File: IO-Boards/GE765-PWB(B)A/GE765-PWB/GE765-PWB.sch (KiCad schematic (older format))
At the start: 55 parts, among them CN33 B12PSHF1A, CN35 B6P-VH, CN36 B3SHF1AA, U1 74LS175, U10 Ferrite_Bead_Small, U11 Ferrite_Bead_Small, U12 Ferrite_Bead_Small, U13 Ferrite_Bead_Small, U17 Ferrite_Bead_Small, U18 Ferrite_Bead_Small, U19 Ferrite_Bead_Small, U2 74LS175, U20 Ferrite_Bead_Small, U21 Ferrite_Bead_Small, U3 74LS14

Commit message: Updated GE765
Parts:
- added C1: 10uf 16v, Capacitor_THT:CP_Radial_D5.0mm_P2.50mm, symbol Device:CP_Small
- added C3: 0.01uf, Capacitor_THT:C_Disc_D3.0mm_W1.6mm_P2.50mm, symbol Device:C_Small
- added J?: Conn_02x40_Row_Letter_First, symbol Connector_Generic:Conn_02x40_Row_Letter_First
- added R1: 510, Resistor_THT:R_Axial_DIN0204_L3.6mm_D1.6mm_P5.08mm_Horizontal, symbol Device:R_Small
- added R13: 4.7k, Resistor_THT:R_Axial_DIN0204_L3.6mm_D1.6mm_P5.08mm_Horizontal, symbol Device:R_Small
- added R2: 470, Resistor_THT:R_Axial_DIN0204_L3.6mm_D1.6mm_P5.08mm_Horizontal, symbol Device:R_Small
- added U?: MPD4701AG, symbol MOSFET_NEC:MPD4701AG
- 8G: renamed from 8D; value 74LS245 -> 74LCX245
- renumbered U2 to 11C, U1 to 8B
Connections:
- net labels added: 11C-CP, 175-~RST, 6D-CLK-1, 6D-CLK-2, 8B-CP, D0, D1, D2, D3, D4, D5, D6, D7, DQ0, DQ1, DQ2, DQ3, DQ4, DQ5, DQ6, DQ7
- wire segments 128 -> 217
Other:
- moved on the sheet: 10D, 11C, 6D1A, 6D1B, 6D1C, 6D1E, 6D1F, 7B, 8B, 8D, 8G, RN2

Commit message: 50% Complete schematics
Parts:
- added R12: 4.7k, Resistor_THT:R_Axial_DIN0204_L3.6mm_D1.6mm_P5.08mm_Horizontal, symbol Device:R_Small
- RA2: renamed from RN2; value R_Network08 -> 4.7K
- RA4: renamed from RN3; value R_Network08 -> 4.7k
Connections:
- net labels added: 8G-A~B, 8G-~CE, CN31-A15, CN31-A21, CN31-A22, CN31-A6, CN31-B21, CN31-B22, CN31-B23, CN31-B6, D4701-RESET, D4701-U~L, D4701-~CE, D4701-~X~Y
- wire segments 217 -> 266
- no-connect marks 1 -> 28
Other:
- note added: "Output 1"
- note added: "Output 2"
- note added: "Output Driver 1"
- note added: "Output Driver 2"
- moved on the sheet: 10D, 11C, 2G, 3G, 4G, 6D1A, 6D1B, 6D1C, 6D1D, 6D1E, 6D1F, 6E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

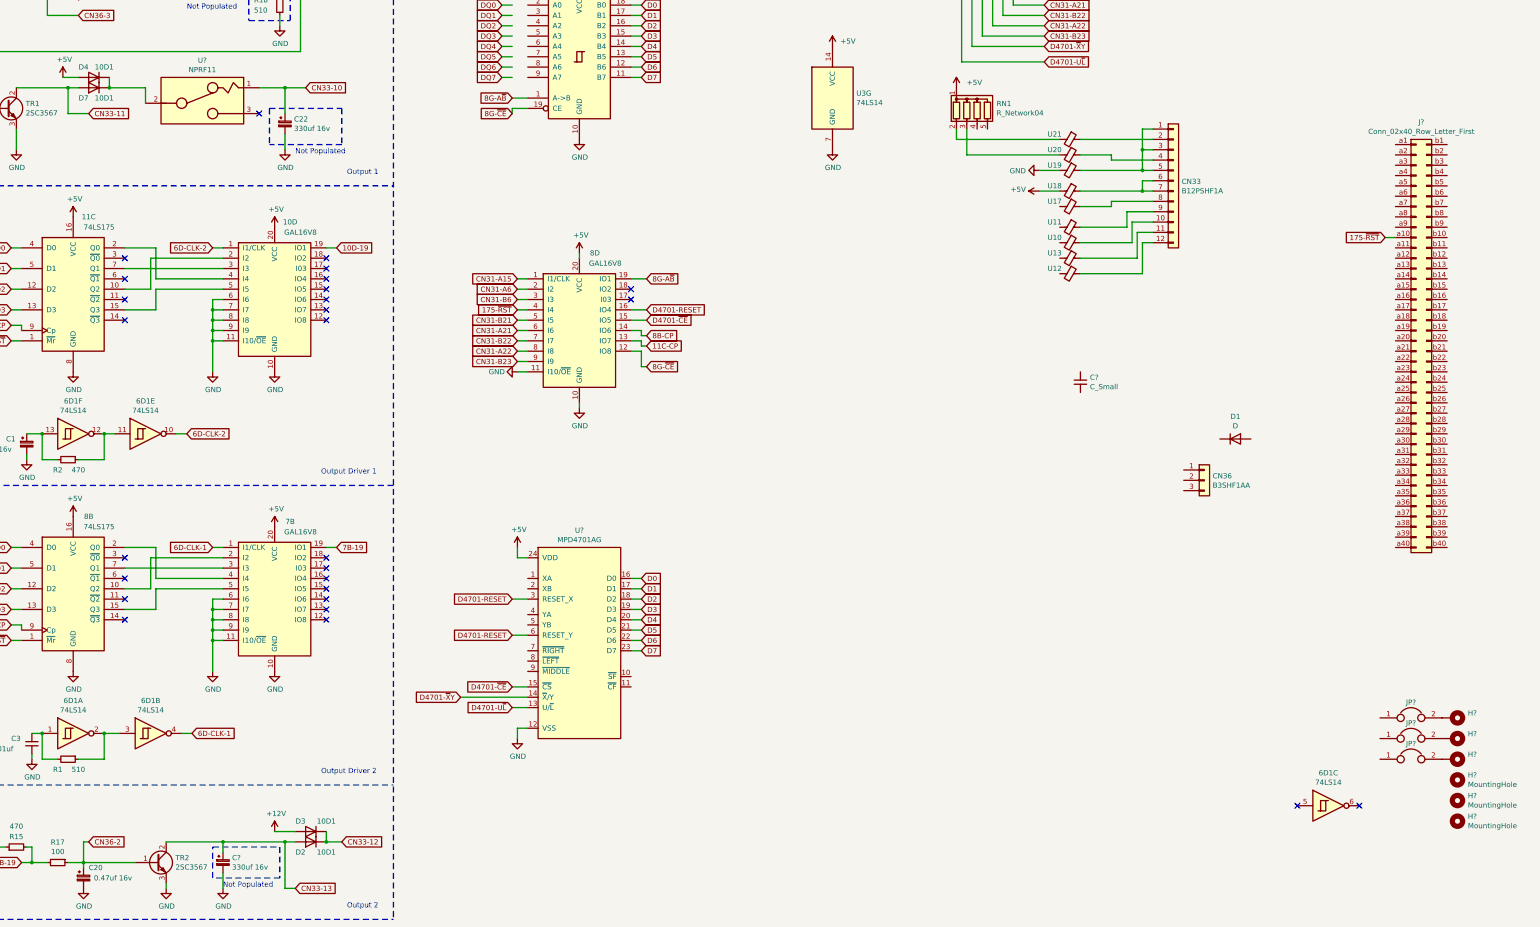
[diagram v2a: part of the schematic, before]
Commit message: Finished reel connector
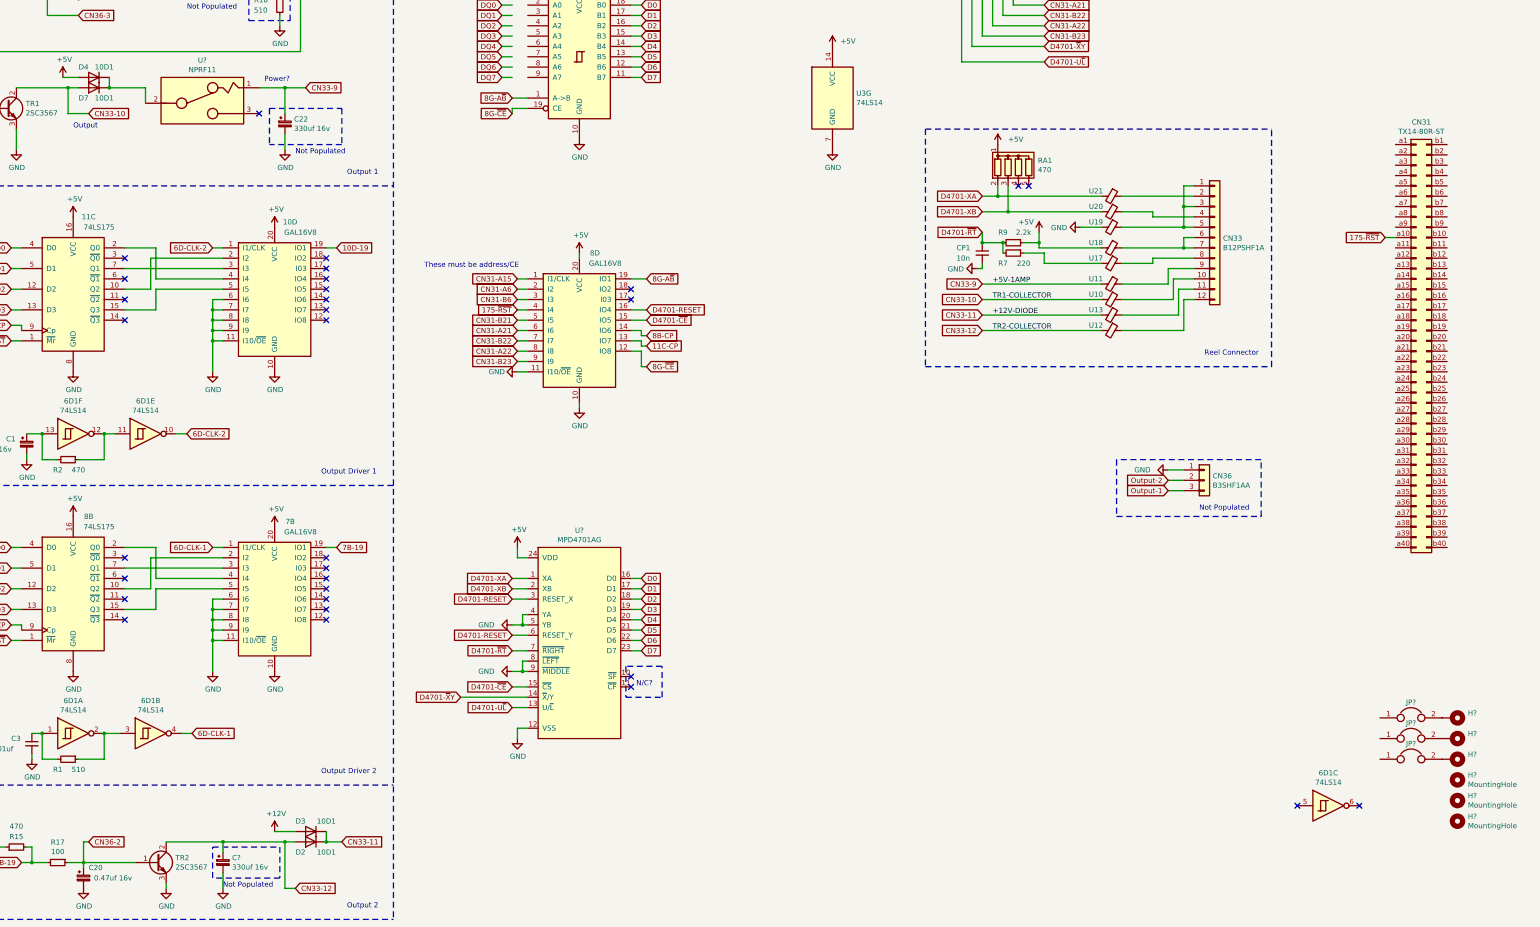
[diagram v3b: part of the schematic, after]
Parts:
- removed C?: C_Small, symbol Device:C_Small
- removed D1: D, Diode_THT:D_A-405_P10.16mm_Horizontal, symbol Device:D
- added CP1: 10n, Capacitor_THT:C_Axial_L3.8mm_D2.6mm_P10.00mm_Horizontal, symbol Device:C_Small
- added R7: 220, Resistor_THT:R_Axial_DIN0204_L3.6mm_D1.6mm_P5.08mm_Horizontal, symbol Device:R_Small
- added R9: 2.2k, Resistor_THT:R_Axial_DIN0204_L3.6mm_D1.6mm_P5.08mm_Horizontal, symbol Device:R_Small
- CN31: renamed from J?; value Conn_02x40_Row_Letter_First -> TX14-80R-ST
- RA1: renamed from RN1; value R_Network04 -> 470
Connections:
- net CN33-13 is gone; now on net CN33-12: C?.1, D2.2 (A), TR2.2 (C)
- net +5V: now also R9.1
- net CN33-10: now also D7.2 (A), TR1.2 (C), U10.2; no longer C22.1, U?.1
- net CN33-11: now also D2.1 (K), D3.1 (K), U13.2; no longer D7.2 (A), TR1.2 (C)
- net CN33-12: now also U12.2; no longer D2.1 (K), D3.1 (K)
- net GND: now also CN36.1 (Pin_1), U?.4 (YA), U?.5 (YB), U?.8 (~LEFT), U?.9 (~MIDDLE), CP1.2
- net Output-2: now reaches CN36.2 (Pin_2)
- net Output-1: now reaches CN36.3 (Pin_3)
- net D4701-XA: now reaches U?.1 (XA)
- net D4701-XA: now also RA1.2 (R1), U21.2
- net D4701-XB: now reaches U?.2 (XB)
- net D4701-XB: now also RA1.3 (R2), U20.2
- net D4701-~RT: now reaches U?.7 (~RIGHT)
- net D4701-~RT: now also CP1.1, R7.2, R9.2
- net CN33-9: now reaches U11.2
- net CN33-9: now also C22.1, U?.1
- net at U17.2: now also R7.1
- no-connect marks 28 -> 32
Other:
- note added: "N/C?"
- note added: "Output"
- note added: "Power?"
- note added: "Reel Connector"
- note added: "These must be address/CE"
- moved on the sheet: CN33, RA1, U10, U11, U12, U13, U17, U18, U19, U20, U21

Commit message: More CN31 connector labels
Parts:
- added C15: 100uf 16v, Capacitor_THT:CP_Radial_D5.0mm_P2.50mm, symbol Device:CP_Small
- renumbered RA4 to RA3
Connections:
- net +5V: no longer 8G.20 (VCC), RA3.1 (common)
- net 175-~RST: no longer 11C.1 (~Mr), 8B.1 (~Mr), 8D.4 (I4), CN31.a10 (Pin_a10)
- net CN31-A15: no longer 8D.1 (I1/CLK)
- net DQ0: now also 8G.2 (A0), CN31.a32 (Pin_a32)
- net DQ1: now also 8G.3 (A1), CN31.b32 (Pin_b32)
- net DQ2: now also 8G.4 (A2), CN31.a31 (Pin_a31)
- net DQ3: now also 8G.5 (A3), CN31.b31 (Pin_b31)
- net DQ4: now also 8G.6 (A4), CN31.a30 (Pin_a30)
- net DQ5: now also 8G.7 (A5), CN31.b30 (Pin_b30)
- net DQ6: now also 8G.8 (A6), CN31.a29 (Pin_a29)
- net DQ7: now also 8G.9 (A7), CN31.b29 (Pin_b29)
- net GND: now also CN31.a11 (Pin_a11), CN31.a13 (Pin_a13), CN31.a33 (Pin_a33), CN31.a34 (Pin_a34), CN31.a35 (Pin_a35), CN31.a8 (Pin_a8), CN31.a9 (Pin_a9), CN31.b11 (Pin_b11), CN31.b13 (Pin_b13), CN31.b33 (Pin_b33), CN31.b34 (Pin_b34), CN31.b35 (Pin_b35), CN31.b9 (Pin_b9), C15.2
- net CN31-5V: now reaches CN31.a1 (Pin_a1)
- net CN31-5V: now also CN31.a2 (Pin_a2), CN31.a3 (Pin_a3), CN31.a4 (Pin_a4), CN31.a5 (Pin_a5), CN31.b1 (Pin_b1), CN31.b2 (Pin_b2), CN31.b3 (Pin_b3), CN31.b4 (Pin_b4), CN31.b5 (Pin_b5)
- net DQ14: now reaches CN31.a25 (Pin_a25)
- net DQ12: now reaches CN31.a26 (Pin_a26)
- net DQ10: now reaches CN31.a27 (Pin_a27)
- net DQ8: now reaches CN31.a28 (Pin_a28)
- net CN31-3V3: now reaches CN31.a36 (Pin_a36)
- net CN31-3V3: now also 8G.20 (VCC), CN31.a37 (Pin_a37), CN31.a38 (Pin_a38), CN31.a39 (Pin_a39), CN31.a40 (Pin_a40), CN31.b36 (Pin_b36), CN31.b37 (Pin_b37), CN31.b38 (Pin_b38), CN31.b39 (Pin_b39), CN31.b40 (Pin_b40), RA3.1 (common), C15.1
- net DQ15: now reaches CN31.b25 (Pin_b25)
- net DQ13: now reaches CN31.b26 (Pin_b26)
- net DQ11: now reaches CN31.b27 (Pin_b27)
- net DQ9: now reaches CN31.b28 (Pin_b28)
- net CN31-A6 renamed CN31-A6-READ?
- net CN31-B6 renamed CN31-B6-WRITE?
- new net CN31-A15-CE?: 8D.1 (I1/CLK)
- new net ~IO_RESET: 11C.1 (~Mr), 8B.1 (~Mr), 8D.4 (I4), CN31.a10 (Pin_a10)
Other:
- note added: "These must be address/CE/RD/WR"
- note removed: "These must be address/CE"
